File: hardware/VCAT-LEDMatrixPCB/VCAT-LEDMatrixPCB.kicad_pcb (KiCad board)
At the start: 2 copper layers, 144.3 x 54.6 mm, 173 parts, among them IC4 AP64501QSP-13, J1 Conn_01x03

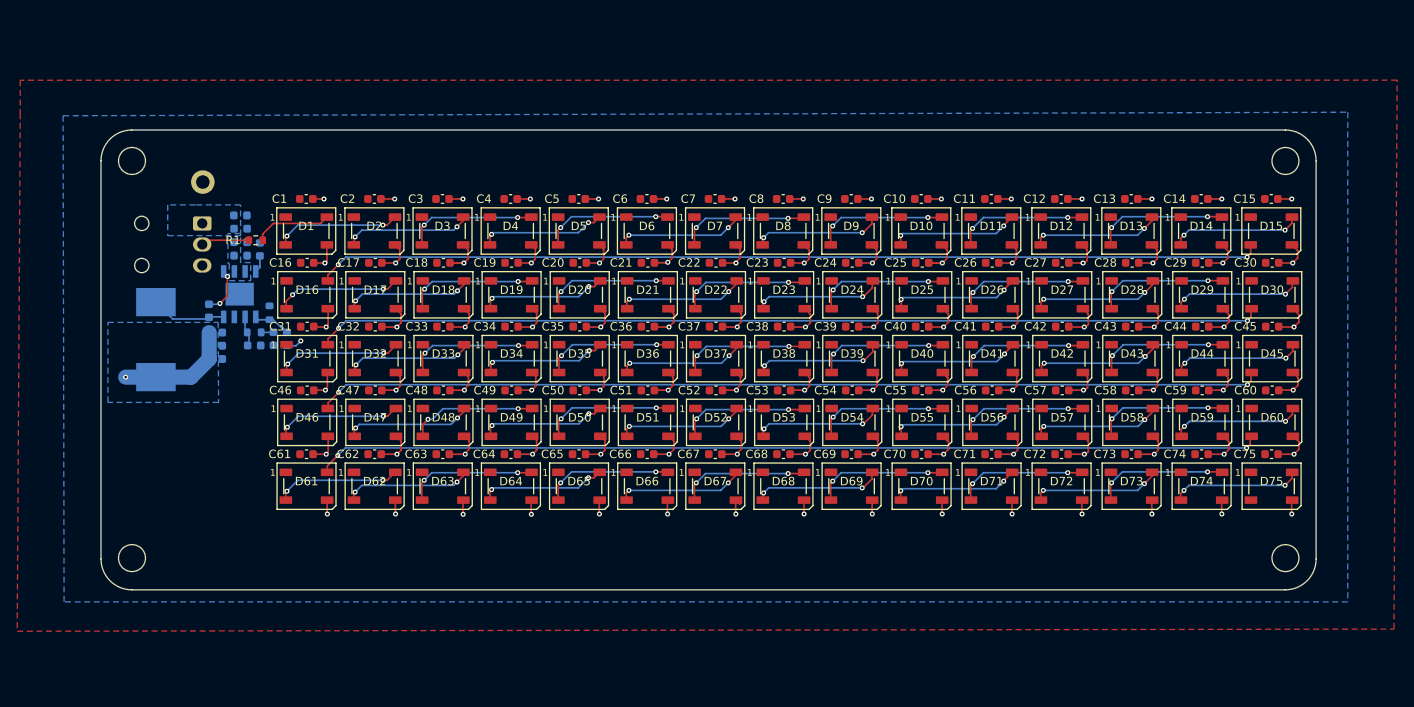
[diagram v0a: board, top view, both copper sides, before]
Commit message: Added Vias and made board symmetrical
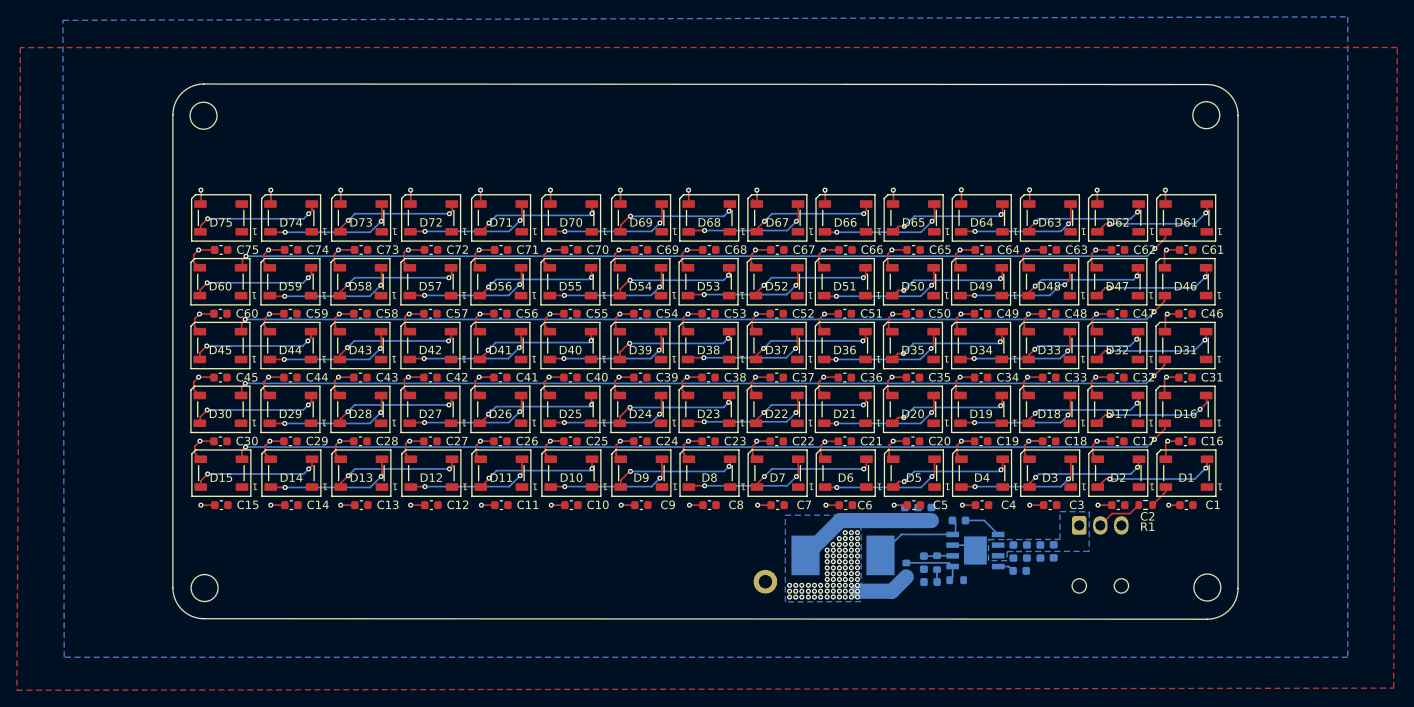
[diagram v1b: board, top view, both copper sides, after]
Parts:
- removed the H1 at (73.9, 21.5)
- added H4: MountingHole, MountingHole:MountingHole_3.2mm_M3, F.Cu at (201.5, 16.1)
- moved H2 138.0 mm to (82.5, 72.2), turned to -90 degrees
- moved C15 129.8 mm to (84.5, 62.3), turned to 180 degrees
- moved D75 128.7 mm to (84.5, 28.2), turned to 180 degrees
- moved D15 127.9 mm to (84.5, 58.5), turned to 180 degrees
- moved C75 127.0 mm to (84.5, 32.0), turned to 180 degrees
- moved C30 126.7 mm to (84.4, 54.8), turned to 180 degrees
- moved D60 126.0 mm to (84.4, 35.8), turned to 180 degrees
- moved D30 125.6 mm to (84.4, 51.0), turned to 180 degrees
- moved C60 125.2 mm to (84.4, 39.6), turned to 180 degrees
- moved C45 125.0 mm to (84.4, 47.2), turned to 180 degrees
- moved D45 124.9 mm to (84.4, 43.4), turned to 180 degrees
- moved C14 114.0 mm to (92.8, 62.3), turned to 180 degrees
- moved D74 112.7 mm to (92.8, 28.2), turned to 180 degrees
- moved D14 111.8 mm to (92.8, 58.5), turned to 180 degrees
- moved C74 110.8 mm to (92.8, 32.0), turned to 180 degrees
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- renumbered H4 to H1
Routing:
- net +5V: track 16.1 -> 23.2 mm, vias 2 -> 84
- net Net-(D1-DIN): track 9.19 -> 2.78 mm
- net GND: track 307.8 -> 310.7 mm
- net Net-(IC4-FB): track 4.57 -> 7.45 mm
- net Net-(IC4-SW): track 8.98 -> 11.6 mm
- net Net-(IC4-BST): track 5.69 -> 4.57 mm, vias 2 -> 0
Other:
- board size 144.3 x 54.6 mm -> 126.5 x 63.5 mm

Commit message: Review without Bom
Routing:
- net +5V: vias 84 -> 114

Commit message: overall review
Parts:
- moved TP2 51.1 mm to (199.8, 65.5)
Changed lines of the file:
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@@
 	(footprint "TestPoint:TestPoint_Keystone_5005-5009_Compact"
 		(layer "B.Cu")
-		(at 149.11 71.44)
+		(at 199.82 65.53)
 		(descr "Keystone THM Compact Test Point 5005-5009, http://www.keyelco.com/product-pdf.cfm?p=1314")
 		(tags "Through Hole Mount Test Points")
 		(property "Reference" "TP2"
-			(at 0 -2.65 180)
+			(at -0.01 2.65 180)
 			(layer "B.SilkS")
 			(effects
